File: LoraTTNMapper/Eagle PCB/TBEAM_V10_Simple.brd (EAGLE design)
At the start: 100 x 80 mm, 28 parts, among them IC1 L298, IC2 ULN2003AD, J1 1X2-3.5MM, J2 1X2-3.5MM, J3 1X2-3.5MM

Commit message: pcb layout
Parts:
- removed C1, C2: 100nF, rcl:C050-024X044
- removed D1, D2, D3, D4, D5, D6, D7, D8: (no value), diode:D-5
- removed IC1: L298, st-microelectronics:MULTIWATT-15
- removed J1, J2, J3: 1X2-3.5MM, adafruit:1X2-3.5MM
- added BATTERY_SWITCH: (no value), pinhead:1X02
- added BAT_IN, BAT_OUT: (no value), wirepad:SMD2,54-5,08
- added U$2: DC-DC-STEP-DOWN-LM2596, diy-modules:DC-DC-STEP-DOWN-LM2596
- added X1: (no value), con-berg:PN87520
- moved SERVO_1 69.9 mm to (5.08, 29.2), turned to 90 degrees
- moved SERVO_2/GPIO32 63.8 mm to (5.08, 39.4), turned to 90 degrees
- moved LED2 63.5 mm to (12.7, 30.5), turned to 270 degrees
- moved LED3 56.9 mm to (12.7, 40.6), turned to 270 degrees
- moved R2 56.2 mm to (16.5, 30.5), turned to 90 degrees
- moved R3 50.4 mm to (16.5, 40.6), turned to 90 degrees
- moved SOLAR_IN 41.3 mm to (95.2, 49.5), turned to 270 degrees
- moved LED1 37.0 mm to (54.6, 43.2), turned to 180 degrees
- moved INA219 35.7 mm to (35.6, 29.2), turned to 180 degrees
- moved R1 35.6 mm to (54.6, 38.1), turned to 0 degrees
- moved OLED_DISPLAY 30.2 mm to (61.0, 72.4)
- moved BME280 14.5 mm to (59.7, 39.4), turned to 90 degrees
- moved IC2 6.48 mm to (36.8, 39.4)
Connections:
- removed net N$2: IC2.16, SERVO_1.1, SERVO_2/GPIO32.1
- removed net N$7: D1.A, D2.C, IC1.2, J2.1
- removed net V+: C2.1, D1.C, D3.C, D5.C, D6.C, IC1.4, J1.1
- new net POWER_RAIL_1_VDD: IC2.14, IC2.15, IC2.16, SERVO_1.1, SERVO_2/GPIO32.1
- net +5V: no longer C1.1, IC1.9
- net GND: now also U$2.IN-, U$2.OUT-, X1.4; no longer C1.2, C2.2, D2.A, D4.A, D7.A, D8.A, IC1.1, IC1.15, IC1.8, J1.2
- net GPIO15: now also IC2.2, IC2.3
- net N$10: now also BATTERY_SWITCH.2, BAT_OUT.1; no longer D5.A, D7.C, IC1.13, J3.1
- net N$8: now also U$2.OUT+, X1.1; no longer D3.A, D4.C, IC1.3, J2.2
- net N$9: now also BATTERY_SWITCH.1, BAT_IN.1; no longer D6.A, D8.C, IC1.14, J3.2
- net V_OUT_+: now also U$2.IN+
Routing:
- net GND: track 0.00 -> 306.5 mm
- net VDD: track 0.00 -> 121.7 mm
- net SDA: track 0.00 -> 103.3 mm
- net SCL: track 0.00 -> 97.3 mm
- net VDD_SWITCHABLE: track 0.00 -> 77.2 mm
- net V_IN_+: track 0.00 -> 61.5 mm
- net GPIO15: track 0.00 -> 58.2 mm
- net POWER_RAIL_1_VDD: track 0.00 -> 44.1 mm
- net GPIO35: track 0.00 -> 35.4 mm
- net V_OUT_+: track 0.00 -> 22.1 mm
- net GPIO32: track 0.00 -> 21.6 mm
- net N$8: track 0.00 -> 15.7 mm
- net N$9: track 0.00 -> 7.40 mm
- net N$10: track 0.00 -> 7.40 mm
- net N$4: track 0.00 -> 5.21 mm
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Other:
- board text added: "+18V"
- board text added: "Data"
- board text removed: "+"
- board text removed: "+ 3-12Volt"
- board text removed: "-"
- board text removed: "Motor 1"
- board text removed: "Motor 2"
- board text removed: "Power Motor"

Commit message: PCB
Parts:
- added GPIO04: FAST LED, pinhead:1X03
- added GPIO_BUS: (no value), pinhead:1X08
- added I2C, I2C1: (no value), pinhead:1X04
- added LED4: VDD Switchable, led:SML1206
- added POWER_RAIL2, V5: (no value), con-wago-500:W237-102
- added R4: 220, resistor:R1206
- LED2: value (none) -> GPIO35
- LED3: value (none) -> GPIO32
- R1, R2, R3: value (none) -> 220
- moved BATTERY_SWITCH 26.9 mm to (74.9, 49.5)
- moved R1 25.5 mm to (57.1, 63.5), turned to 90 degrees
- moved LED1 9.92 mm to (48.3, 35.6)
- moved BME280 5.39 mm to (63.5, 35.6)
- moved BAT_IN 5.08 mm to (74.9, 68.6)
- moved BAT_OUT 3.81 mm to (83.8, 68.6)
- moved INA219 3.81 mm to (35.6, 25.4), turned to 0 degrees
- moved LED3 2.84 mm to (10.2, 41.9), turned to 0 degrees
- moved LED2 2.54 mm to (10.2, 30.5), turned to 0 degrees
- moved R2 1.80 mm to (15.2, 31.8)
- moved IC2 1.80 mm to (38.1, 38.1)
- moved R3 1.27 mm to (15.2, 40.6), turned to 270 degrees
- moved SERVO_1 1.27 mm to (5.08, 27.9)
- moved U$2 1.27 mm to (76.2, 11.4)
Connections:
- removed net POWER_RAIL_1_VDD: IC2.14, IC2.15, IC2.16, SERVO_1.1, SERVO_2/GPIO32.1
- new net GPIO02: GPIO_BUS.5, U$1.11
- new net GPIO04: GPIO04.1, U$1.23
- new net GPIO13: GPIO_BUS.4, U$1.10
- new net GPIO14: GPIO_BUS.3, U$1.9
- new net GPIO25: GPIO_BUS.2, U$1.8
- new net GPIO33: GPIO_BUS.1, U$1.7
- new net GPIO36: IC2.4, IC2.5, IC2.6, IC2.7, U$1.1
- new net N$11: LED4.A, R4.1
- new net N$12: IC2.10, IC2.11, IC2.12, IC2.13, POWER_RAIL2.2
- new net POWER_RAIL_1_GND: GPIO_BUS.6, IC2.14, IC2.15, IC2.16, SERVO_1.1, SERVO_2/GPIO32.1
- net +5V: now also GPIO04.2, IC2.9, POWER_RAIL2.1, SERVO_1.2, SERVO_2/GPIO32.2
- net GND: now also GPIO04.3, GPIO_BUS.7, I2C.3, I2C1.3, LED4.C, V5.1
- net N$8: now also V5.2
- net SCL: now also I2C.2, I2C1.2, U$1.18; no longer U$1.17
- net SDA: now also I2C.1, I2C1.1, U$1.17; no longer U$1.18
- net VDD: now also GPIO_BUS.8; no longer IC2.9, SERVO_1.2, SERVO_2/GPIO32.2
- net VDD_SWITCHABLE: now also I2C.4, I2C1.4, R4.2
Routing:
- net GND: track 306.5 -> 0.00 mm
- net VDD: track 121.7 -> 0.00 mm
- net SDA: track 103.3 -> 0.00 mm
- net SCL: track 97.3 -> 0.00 mm
- net VDD_SWITCHABLE: track 77.2 -> 0.00 mm
- net V_IN_+: track 61.5 -> 0.00 mm
- net GPIO15: track 58.2 -> 0.00 mm
- net POWER_RAIL_1_VDD: track 44.1 -> 0.00 mm
- net GPIO35: track 35.4 -> 0.00 mm
- net V_OUT_+: track 22.1 -> 0.00 mm
- net GPIO32: track 21.6 -> 0.00 mm
- net N$8: track 15.7 -> 0.00 mm
- net N$9: track 7.40 -> 0.00 mm
- net N$10: track 7.40 -> 0.00 mm
- net N$4: track 5.21 -> 0.00 mm
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- added copper zone on layer 1, net GND
- added copper zone on layer 16, net GND
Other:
- board text added: "+5v"
- board text added: "---------------------------------- GPIO 04 = FAST Led GPIO 15 = Power Rail 1 GPIO 35 = Servo 1 GPIO 32 = Servo 2 GPIO 36 = Power Rail 2 ---------------------------------"
- board text added: "DC Converter Out 3-18V"
- board text added: "DC DC Buck Converter LM2596"
- board text added: "GPIO02"
- board text added: "GPIO04"
- board text added: "GPIO13"
- board text added: "GPIO14"
- board text added: "GPIO15"
- board text added: "GPIO25"
- board text added: "GPIO32"
- board text added: "GPIO33"
- board text added: "GPIO35"
- board text added: "Lora TTN Solar Board (C) Jochen Szaroletta 2021"
- board text added: "Power Rail"
- board text added: "Power Rail 2"
- board text added: "SOLAR IN"
- board text added: "Servo 1"
- board text added: "Servo 2"
- board text added: "ULN2003"
- board text added: "VDD Power Rail"
- board text added: "Vin 6-18V"
- board text added: "Vin+"
- board text added: "Vin-"
- board text added: "https://github.com/MrFlexi/LoraTTNMapper"
- board text removed: "+18V"
- board text removed: "Data"

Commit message: updates
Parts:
- added LED5, LED6, LED7, LED8, LED9: Power Rail, led:SML1206
- added R5, R6, R7, R8, R9: 470, resistor:R0603
- R1, R2, R3, R4: value 220 -> 470; device resistor:R1206 -> resistor:R0603
- moved R1 53.2 mm to (27.9, 19.1), turned to 180 degrees
- moved R4 51.4 mm to (36.8, 20.3), turned to 0 degrees
- moved GPIO04 18.2 mm to (29.2, 10.2)
- moved GPIO_BUS 17.8 mm to (12.7, 2.54)
- moved I2C1 7.18 mm to (16.5, 20.3)
- moved I2C 7.18 mm to (16.5, 25.4)
- moved R2 1.27 mm to (15.2, 30.5), turned to 0 degrees
- moved LED1 1.27 mm to (48.3, 36.8)
- moved R3 1.27 mm to (15.2, 41.9), turned to 0 degrees
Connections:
- new net GPIO39: GPIO_BUS.1, R5.2, U$1.2
- new net N$13: LED5.A, R5.1
- new net N$14: U$1.3
- new net N$15: LED6.A, R6.1
- new net N$16: LED7.A, R7.1
- new net N$17: LED8.A, R8.1
- new net N$18: LED9.A, R9.2
- net GND: now also LED5.C, LED6.C, LED7.C, LED8.C, LED9.C
- net GPIO02: now also GPIO04.1, R8.2
- net GPIO04: now also R3.2, SERVO_2/GPIO32.3; no longer GPIO04.1
- net GPIO13: now also R2.2, SERVO_1.3
- net GPIO14: now also R7.2
- net GPIO25: now also R6.2
- net GPIO32: no longer R3.2, SERVO_2/GPIO32.3
- net GPIO33: no longer GPIO_BUS.1
- net GPIO35: no longer R2.2, SERVO_1.3
- net GPIO36: now also R9.1
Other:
- board text added: "13"
- board text added: "14"
- board text added: "2"
- board text added: "25"
- board text added: "39"
- board text added: "GPIO4"
- board text added: "Power Rail 1"
- board text added: "Rail1 GND"
- board text removed: "GPIO02"
- board text removed: "GPIO04"
- board text removed: "GPIO14"
- board text removed: "Power Rail"
- board text removed: "VDD Power Rail"

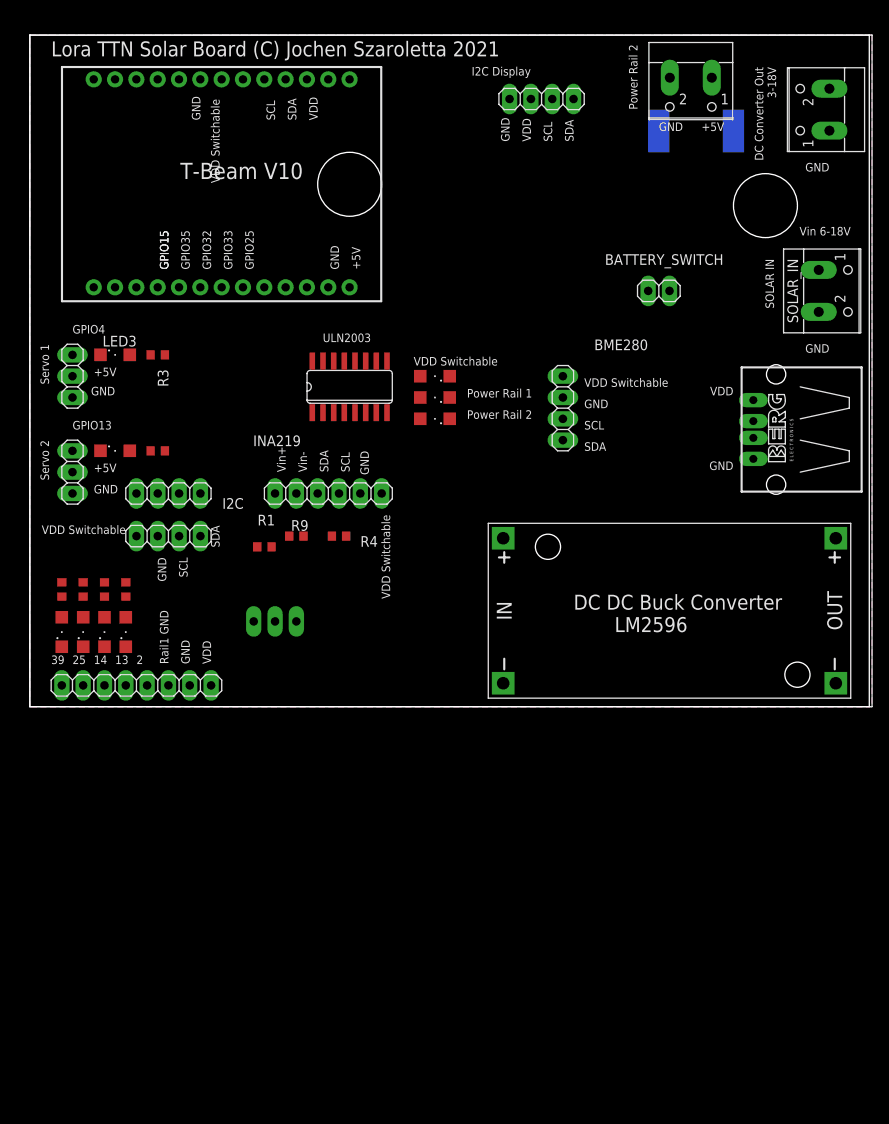
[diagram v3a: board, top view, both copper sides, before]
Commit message: PCB Update P Mosfet to switch Solar Panel
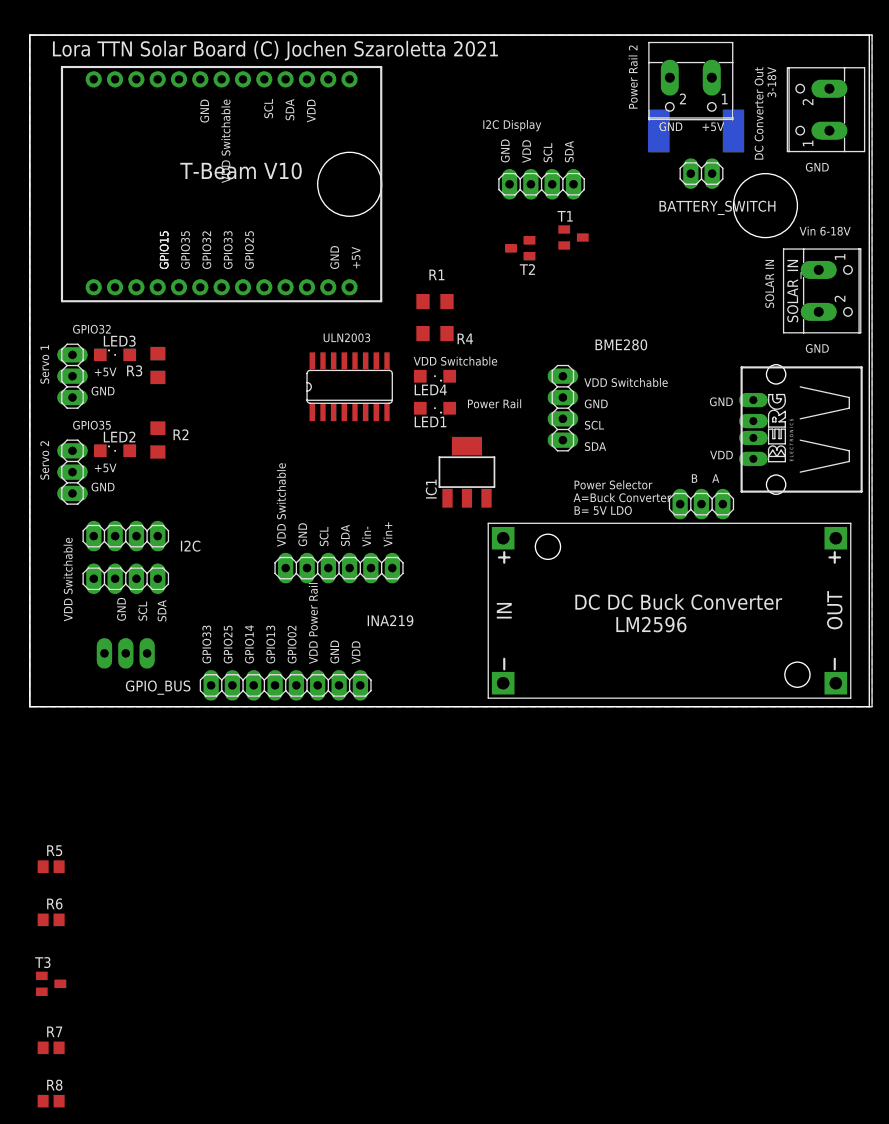
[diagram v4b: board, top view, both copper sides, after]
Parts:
- removed LED5, LED6, LED7, LED8, LED9: Power Rail, led:SML1206
- removed R9: 470, resistor:R0603
- added GPIO01: FAST LED, pinhead:1X03
- added IC1: LT1963EST-1.8, linear-technology:SOT223
- added T1: T_P-MOSFET_AO3401A_ALPHA_SOT23-GSD, JLC PCB Basic Parts_loc:SOT23
- added T2: T_PNP_SS8550-Y2_CHANGJ_SOT23-BEC, JLC PCB Basic Parts_loc:SOT23
- added T3: T_NPN_SS8050_CHANGJ_SOT23-BEC, JLC PCB Basic Parts_loc:SOT23
- R1, R2, R3, R4: value 470 -> 220; device resistor:R0603 -> resistor:R1206
- R5, R6: value 470 -> R_10R_0805; device resistor:R0603 -> JLC PCB Basic Parts_loc:R0805
- R7, R8: value 470 -> R_1.8K_0805; device resistor:R0603 -> JLC PCB Basic Parts_loc:R0805
- moved R8 61.6 mm to (2.54, -47.0), turned to 0 degrees
- moved R7 55.0 mm to (2.54, -40.6), turned to 0 degrees
- moved R6 39.6 mm to (2.54, -25.4), turned to 0 degrees
- moved R1 35.6 mm to (48.3, 48.3)
- moved R5 33.0 mm to (2.54, -19.1), turned to 0 degrees
- moved R4 26.7 mm to (48.3, 44.5)
- moved GPIO04 18.2 mm to (11.4, 6.35)
- moved GPIO_BUS 17.8 mm to (30.5, 2.54)
- moved BATTERY_SWITCH 14.9 mm to (80.0, 63.5)
- moved OLED_DISPLAY 10.2 mm to (61.0, 62.2)
- moved INA219 8.98 mm to (36.8, 16.5), turned to 180 degrees
- moved I2C1 7.18 mm to (11.4, 15.2)
- moved I2C 7.18 mm to (11.4, 20.3)
- moved R2 1.27 mm to (15.2, 31.8), turned to 90 degrees
- moved LED1 1.27 mm to (48.3, 35.6)
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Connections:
- removed net GPIO39: GPIO_BUS.1, R5.2, U$1.2
- new net BUCK-CONVERTER: GPIO01.1, U$2.OUT+
- net GND: now also IC1.2, IC1.4, R5.1, T3.2; no longer LED5.C, LED6.C, LED7.C, LED8.C, LED9.C
- net GPIO02: no longer GPIO04.1, R8.2
- net GPIO04: now also GPIO04.1; no longer R3.2, SERVO_2/GPIO32.3
- net GPIO13: no longer R2.2, SERVO_1.3
- net GPIO14: now also R7.1, R8.1; no longer R7.2
- net GPIO25: no longer R6.2
- net GPIO32: now also R3.2, SERVO_2/GPIO32.3
- net GPIO33: now also GPIO_BUS.1
- net GPIO35: now also R2.2, SERVO_1.3
- net GPIO36: no longer R9.1
- net N$13: now also SOLAR_IN.1, T1.2, T2.2; no longer LED5.A, R5.1
- net N$14: now also GPIO01.3, IC1.3; no longer U$1.3
- net N$15: now also R5.2, T1.1, T2.3; no longer LED6.A, R6.1
- net N$16: now also R6.1, T2.1; no longer LED7.A, R7.1
- net N$17: now also R6.2, T3.3; no longer LED8.A, R8.1
- net N$18: now also R7.2, R8.2, T3.1; no longer LED9.A, R9.2
- net N$8: now also GPIO01.2; no longer U$2.OUT+
- net V_IN_+: now also T1.3; no longer SOLAR_IN.1
- net V_OUT_+: now also IC1.1
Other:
- board text added: "A"
- board text added: "B"
- board text added: "GPIO02"
- board text added: "GPIO04"
- board text added: "GPIO14"
- board text added: "Power Rail"
- board text added: "Power Selector A=Buck Converter B= 5V LDO"
- board text added: "VDD Power Rail"
- board text removed: "13"
- board text removed: "14"
- board text removed: "2"
- board text removed: "25"
- board text removed: "39"
- board text removed: "GPIO4"
- board text removed: "Power Rail 1"
- board text removed: "Rail1 GND"
